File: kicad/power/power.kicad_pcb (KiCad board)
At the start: 2 copper layers, 114.9 x 75.4 mm, 18 parts, among them J1 Conn_01x06, J10 Conn_01x06, J11 Conn_01x06, J12 Conn_01x06, J13 Conn_01x06, J2 AudioJack3, J3 USB_C_Receptacle, J4 AudioJack3, J6 Conn_01x05_Male, J9 Conn_01x04_Male, U1 LM4565F-GE2, U5 LF353DR

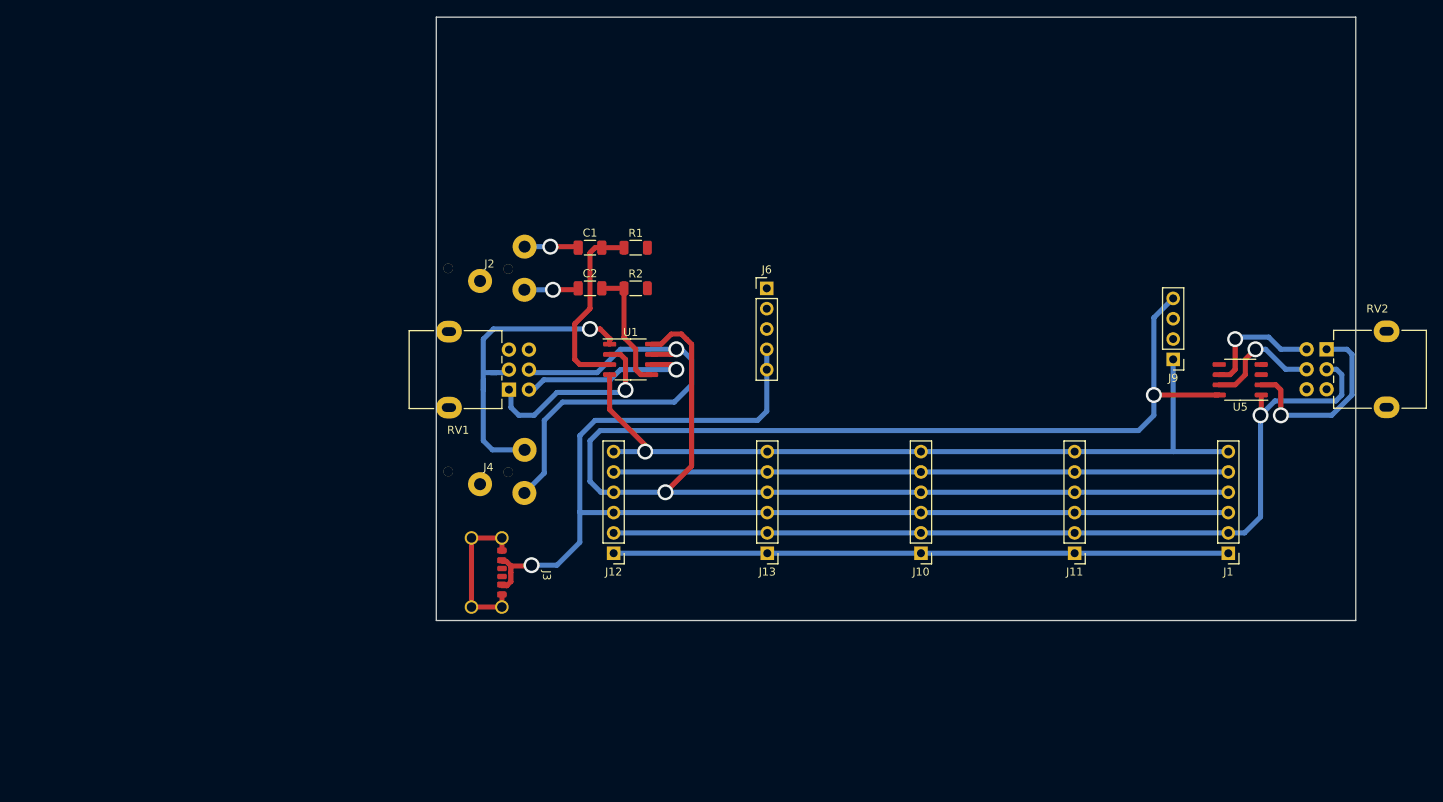
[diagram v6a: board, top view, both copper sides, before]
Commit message: Made new power board
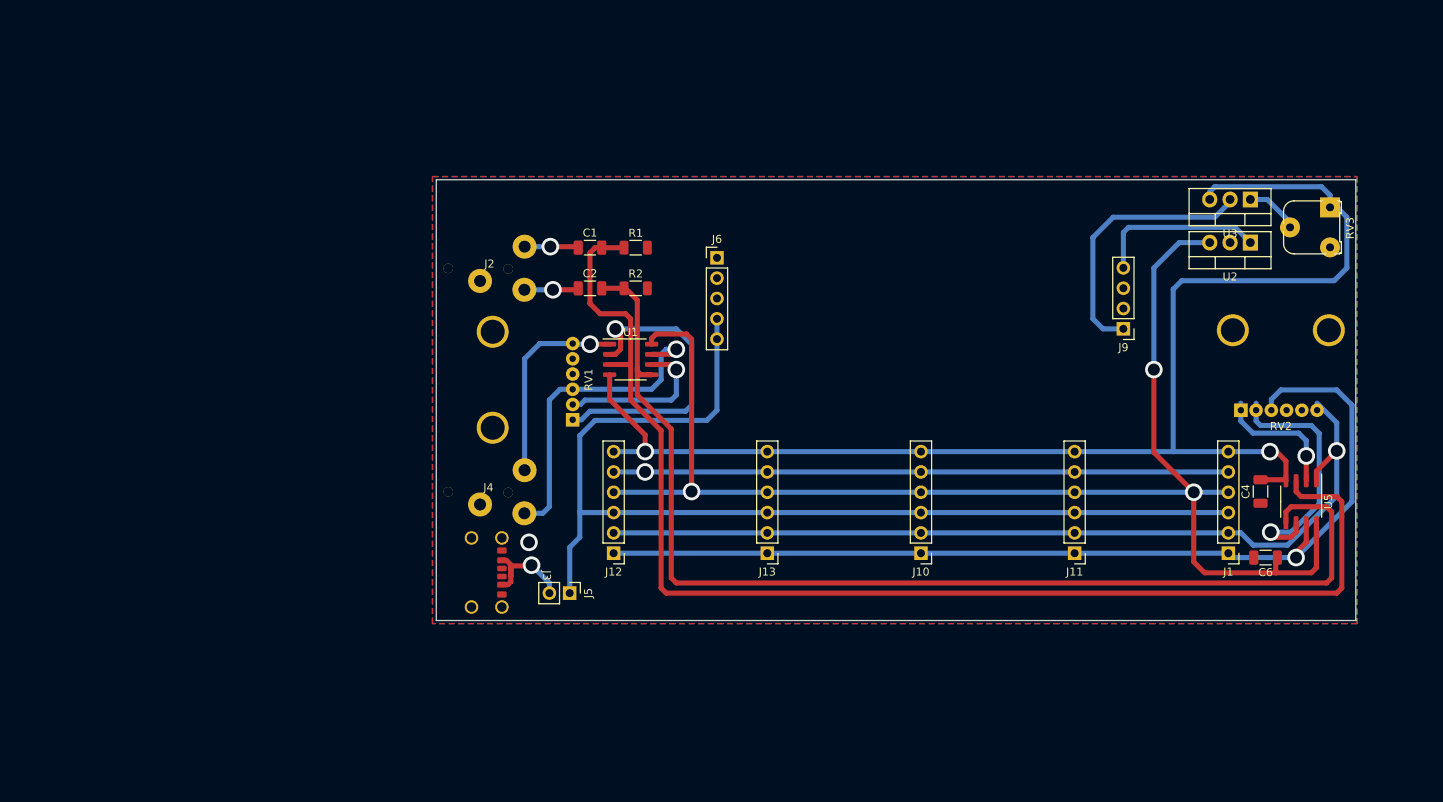
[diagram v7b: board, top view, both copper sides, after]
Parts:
- added C4: C, Capacitor_SMD:C_1206_3216Metric, F.Cu at (191.8, 108.6)
- added C6: C, Capacitor_SMD:C_1206_3216Metric, F.Cu at (192.4, 116.8)
- added J5: Conn_01x02_Male, Connector_PinHeader_2.54mm:PinHeader_1x02_P2.54mm_Vertical, F.Cu at (105.4, 121.3)
- added RV3: R_Potentiometer, Potentiometer_THT:Potentiometer_Runtron_RM-065_Vertical, F.Cu at (200.5, 73.1)
- added U2: LM7812_TO220, Package_TO_SOT_THT:TO-220-3_Vertical, F.Cu at (190.5, 77.5)
- added U3: LM337_TO220, Package_TO_SOT_THT:TO-220-3_Vertical, F.Cu at (190.5, 72.1)
- RV1, RV2: footprint Potentiometer_THT:Potentiometer_Alpha_RD902F-40-00D_Dual_Vertical -> audio_footprint:volume-pot
- moved U5 17.0 mm to (196.8, 109.9), turned to -90 degrees
- moved RV1 10.1 mm to (105.8, 89.6), turned to 90 degrees
- moved RV2 7.65 mm to (199.3, 98.4)
- moved J9 7.30 mm to (174.6, 88.2)
- moved J6 7.30 mm to (123.8, 79.4)
- moved J4 2.54 mm to (95.2, 108.6)
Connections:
- J1 pad 4: +15V -> +12V
- J1 pad 6: -15V -> -12V
- J10 pad 4: +15V -> +12V
- J10 pad 6: -15V -> -12V
- J11 pad 4: +15V -> +12V
- J11 pad 6: -15V -> -12V
- J12 pad 4: +15V -> +12V
- J12 pad 6: -15V -> -12V
- J13 pad 4: +15V -> +12V
- J13 pad 6: -15V -> -12V
- J3 pad A9: +5V -> Net-(J3-PadA4)
- J3 pad B9: +5V -> Net-(J3-PadA4)
- U1 pad 4: -15V -> -12V
- U1 pad 8: +15V -> +12V
- U5 pad 4: -15V -> -12V
- U5 pad 8: +15V -> +12V
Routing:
- net -12V: track 0.00 -> 249.0 mm, vias 0 -> 2
- net +15V: track 264.5 -> 21.4 mm, vias 2 -> 0
- net +12V: track 0.00 -> 230.5 mm, vias 0 -> 3
- net -15V: track 177.1 -> 33.8 mm, vias 1 -> 0
- net audio_in_L: track 23.3 -> 158.6 mm
- net audio_in_R: track 15.8 -> 142.8 mm
- net audio_right: track 168.6 -> 201.0 mm
- net GND: track 172.9 -> 153.5 mm, vias 0 -> 2
- net Net-(J4-PadR): track 58.7 -> 40.5 mm
- net Net-(J4-PadT): track 41.0 -> 25.4 mm
- net Net-(RV2-Pad4): track 16.4 -> 32.0 mm
- net Net-(RV1-Pad1): track 24.0 -> 38.0 mm
- net Net-(J3-PadA4): track 0.00 -> 13.0 mm, vias 0 -> 1
- net +5V: track 218.1 -> 208.0 mm, vias 1 -> 0
- net Net-(RV2-Pad1): track 24.4 -> 16.4 mm
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- added copper zone on B.Cu, net GND
- added copper zone on F.Cu, net GND
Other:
- board size 114.9 x 75.4 mm -> 114.9 x 55.1 mm
